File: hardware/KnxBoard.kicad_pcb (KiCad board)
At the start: 4 copper layers, 29.5 x 33.5 mm, 40 parts, among them J1 Conn_01x10, J2 Conn_01x12, J3 Conn_01x12, J4 Conn_01x02_Male, U1 NCN5130, U2 STM32L432KCUx, X1 FA-238

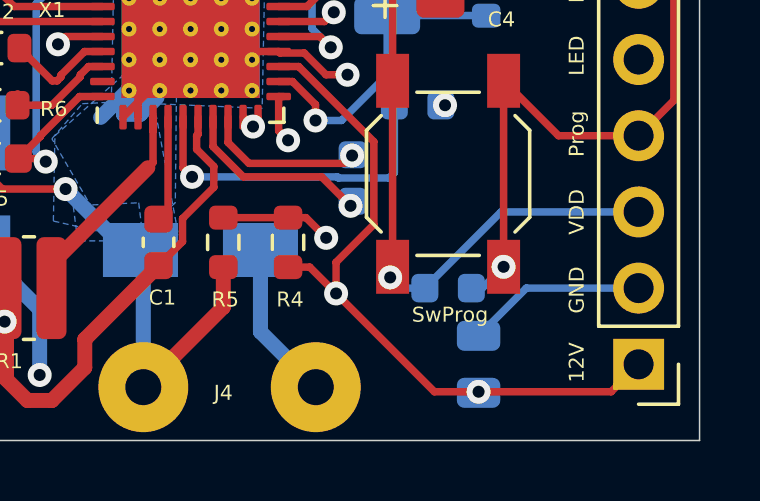
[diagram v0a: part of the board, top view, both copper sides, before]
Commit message: Project: Update to KiCad V6.0
Add also MCO to debug port (TODO: Need to route)
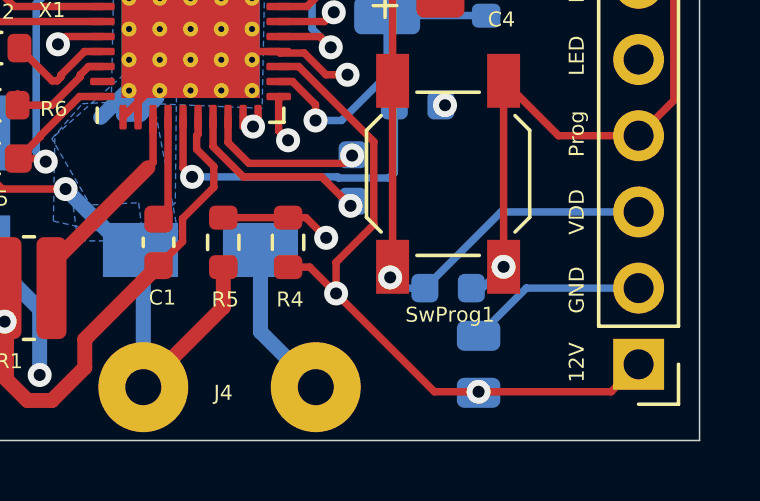
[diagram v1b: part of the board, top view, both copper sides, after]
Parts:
- R22: value 0 -> NOTMOUNT
- renumbered SwProg to SwProg1
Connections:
- J1 pad 8: Net-(J1-Pad8) -> MCO
- J2 pad 1: PC14 -> MCO
- U1 pad 22: Net-(U1-Pad22) -> unconnected-(U1-Pad22)
- U1 pad 39: Net-(U1-Pad39) -> unconnected-(U1-Pad39)
- U2 pad 2: PC14 -> MCO
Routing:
- net PC14: track 4.47 -> 0.00 mm
- net MCO: track 0.00 -> 4.47 mm
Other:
- net class Default removed

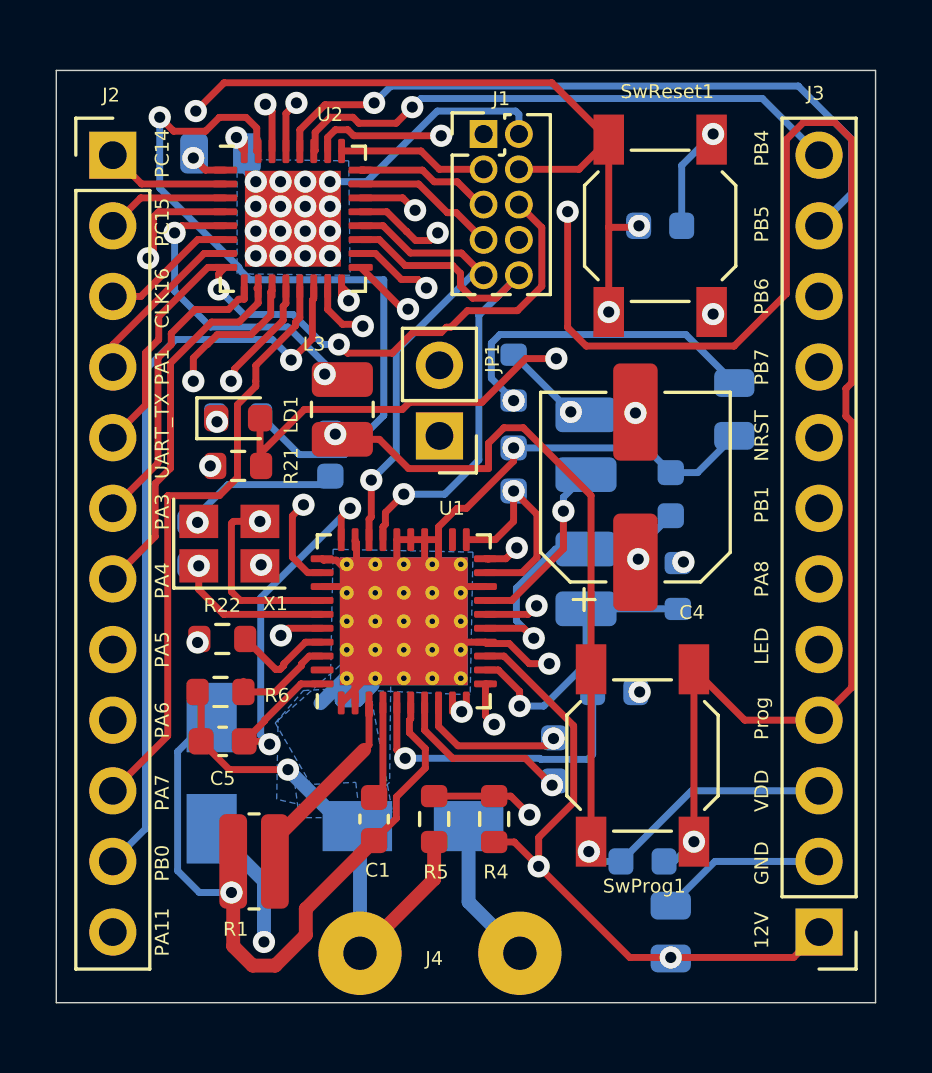
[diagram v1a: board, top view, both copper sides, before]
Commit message: Update pcb rules
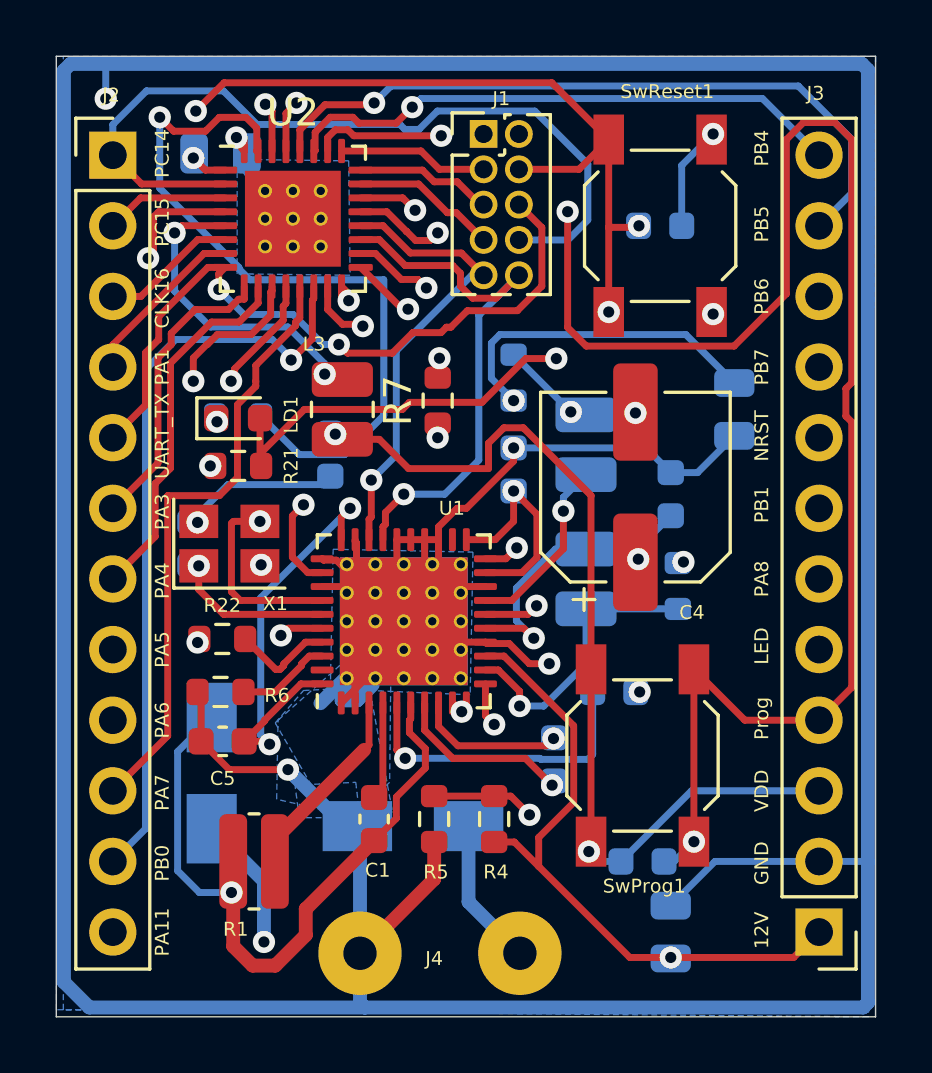
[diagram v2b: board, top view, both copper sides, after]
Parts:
- removed JP1: Jumper_2_Open, Connector_PinHeader_2.54mm:PinHeader_1x02_P2.54mm_Vertical
- added R7: 0, Resistor_SMD:R_0603_1608Metric, F.Cu at (148.8, 102.8)
- U2: footprint Package_DFN_QFN:QFN-32-1EP_5x5mm_P0.5mm_EP3.45x3.45mm -> Package_DFN_QFN:QFN-32-1EP_5x5mm_P0.5mm_EP3.45x3.45mm_ThermalVias
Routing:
- net GND: track 200.2 -> 329.6 mm, vias 28 -> 13
- net MCO: track 4.47 -> 29.6 mm
- net +3V3: track 49.2 -> 47.8 mm, vias 4 -> 5
- net VDD: vias 4 -> 5
- net +12V: vias 3 -> 2
- removed copper zone on In1.Cu, net GND
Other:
- board size 29.5 x 33.5 mm -> 29.5 x 34.5 mm

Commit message: Add CAD file for SMT32U575CIU6Q
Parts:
- added U2: STM32U575CIU6Q, KnxBoard:STM32U575CIU6Q, F.Cu at (143.0, 78.7)
- renumbered U2 to U3

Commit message: Work in progress
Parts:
- removed C21, C23, C5: 100nF 6.3V, Capacitor_SMD:C_0603_1608Metric
- removed C22: 10uF 6.3V ESR < 0.1ohm, Capacitor_SMD:C_0805_2012Metric
- removed C3: 100nF 50V, Capacitor_SMD:C_0603_1608Metric
- removed C41: 1uF 35V ESR < 2ohm, Capacitor_SMD:C_0603_1608Metric
- removed C8, C9: 10pF 6.3V, Capacitor_SMD:C_0603_1608Metric
- removed L3: 220uH, Inductor_SMD:L_1008_2520Metric
- removed R20: 10K 1/16w, Resistor_SMD:R_0603_1608Metric
- removed R22: NOTMOUNT, Resistor_SMD:R_0603_1608Metric
- removed R7: 0, Resistor_SMD:R_0603_1608Metric
- removed SwProg1, SwReset1: SW_Push, Button_Switch_SMD:SW_SPST_SKQG_WithStem
- removed U2: STM32U575CIU6Q, KnxBoard:STM32U575CIU6Q
- removed U3: STM32L432KCUx, Package_DFN_QFN:QFN-32-1EP_5x5mm_P0.5mm_EP3.45x3.45mm_ThermalVias
- added B1: Reset, Button_Switch_SMD:SW_SPST_SKQG_WithStem, F.Cu at (254.0, 104.1)
- added B2: KNX_PROG, Button_Switch_SMD:SW_SPST_SKQG_WithStem, F.Cu at (193.8, 87.4)
- added C12: 1uF 35V ESR < 2ohm, Capacitor_SMD:C_0603_1608Metric_Pad1.08x0.95mm_HandSolder, F.Cu at (219.4, 111.1)
- added C13: 220nF 50V, Capacitor_SMD:C_0603_1608Metric_Pad1.08x0.95mm_HandSolder, F.Cu at (227.6, 97.2)
- added C14: 47nF 50V, Capacitor_SMD:C_0603_1608Metric_Pad1.08x0.95mm_HandSolder, F.Cu at (240.0, 91.5)
- added C15: 100nF 6.3V, Capacitor_SMD:C_0603_1608Metric_Pad1.08x0.95mm_HandSolder, F.Cu at (232.4, 94.2)
- added C16: 10pF 6.3V, Capacitor_SMD:C_0603_1608Metric_Pad1.08x0.95mm_HandSolder, F.Cu at (223.4, 106.2)
- added C17: 10pF 6.3V, Capacitor_SMD:C_0603_1608Metric_Pad1.08x0.95mm_HandSolder, F.Cu at (242.8, 85.2)
- added C18: 100nF 6.3V, Capacitor_SMD:C_0603_1608Metric_Pad1.08x0.95mm_HandSolder, F.Cu at (181.9, 122.9)
- added C19: 10uF 6.3V ESR < 0.1ohm, Capacitor_SMD:C_0805_2012Metric_Pad1.18x1.45mm_HandSolder, F.Cu at (227.9, 94.5)
- added C3_25: 100nF, Capacitor_SMD:C_0603_1608Metric_Pad1.08x0.95mm_HandSolder, F.Cu at (272.5, 87.8)
- added C3_36: 100nF, Capacitor_SMD:C_0603_1608Metric_Pad1.08x0.95mm_HandSolder, F.Cu at (272.5, 85.2)
- added C3_48: 100nF, Capacitor_SMD:C_0603_1608Metric_Pad1.08x0.95mm_HandSolder, F.Cu at (268.2, 93.8)
- added C5_9: 100nF, Capacitor_SMD:C_0603_1608Metric_Pad1.08x0.95mm_HandSolder, F.Cu at (260.9, 102.0)
- added D0: D_Zener, Diode_SMD:D_SOD-323, F.Cu at (268.1, 96.5)
- added JP0: Bootloader, Jumper:SolderJumper-2_P1.3mm_Open_TrianglePad1.0x1.5mm, F.Cu at (255.8, 109.3)
- added JP1: Bootflash, Jumper:SolderJumper-2_P1.3mm_Open_TrianglePad1.0x1.5mm, F.Cu at (268.2, 85.8)
- added JP2: RESETB_NRST, Jumper:SolderJumper-2_P1.3mm_Open_TrianglePad1.0x1.5mm, F.Cu at (251.4, 111.8)
- added JP3: PWR_KNX_MCU, Jumper:SolderJumper-2_P1.3mm_Open_TrianglePad1.0x1.5mm, F.Cu at (200.7, 85.8)
- added TP1: KNX_RXD, TestPoint:TestPoint_Pad_D1.5mm, F.Cu at (185.8, 123.4)
- added TP2: KNX_TXD, TestPoint:TestPoint_Pad_D1.5mm, F.Cu at (190.8, 92.5)
- added U0: STM32U575CIU6Q, KnxBoard:STM32U575CIU6Q, F.Cu at (160.0, 91.4)
- C1: value 47nF 50V -> 100 nF; footprint Capacitor_SMD:C_0603_1608Metric -> Capacitor_SMD:C_0603_1608Metric_Pad1.08x0.95mm_HandSolder
- C10: value 10uF 6.3V ESR < 0.1ohm -> 100nF 50V; footprint Capacitor_SMD:C_0805_2012Metric -> Capacitor_SMD:C_0603_1608Metric_Pad1.08x0.95mm_HandSolder; moved to F.Cu
- C11: value 10uF 6.3V ESR < 0.1ohm -> 100uF 35V; footprint Capacitor_SMD:C_0805_2012Metric -> Capacitor_SMD:CP_Elec_6.3x7.7; moved to F.Cu
- C2: value 220nF 50V -> 10uF; footprint Capacitor_SMD:C_0603_1608Metric -> Capacitor_SMD:C_0603_1608Metric_Pad1.08x0.95mm_HandSolder; moved to F.Cu
- C20: value 100nF 6.3V -> 10uF 6.3V ESR < 0.1ohm; footprint Capacitor_SMD:C_0603_1608Metric -> Capacitor_SMD:C_0805_2012Metric_Pad1.18x1.45mm_HandSolder; moved to F.Cu
- C4: value 100uF 35V -> 1uF; footprint Capacitor_SMD:CP_Elec_6.3x7.7 -> Capacitor_SMD:C_0603_1608Metric_Pad1.08x0.95mm_HandSolder
- C6: value 100nF 6.3V -> 100nF; footprint Capacitor_SMD:C_0603_1608Metric -> Capacitor_SMD:C_0603_1608Metric_Pad1.08x0.95mm_HandSolder; moved to F.Cu
- D1, D2, L1, L2: moved to F.Cu
- J2, J3: value Conn_01x12 -> Conn_01x14; footprint Connector_PinHeader_2.54mm:PinHeader_1x12_P2.54mm_Vertical -> Connector_PinHeader_2.54mm:PinHeader_1x14_P2.54mm_Vertical
- R1: value 27R 1W -> NOTMOUNT; footprint Resistor_SMD:R_0612_1632Metric -> Resistor_SMD:R_0603_1608Metric
- R2: value 1R 1/16W -> 56K 1/16w; moved to F.Cu
- R3: value 1R 1/16W -> 499K 1/16w; moved to F.Cu
- R4: value 56K 1/16w -> 1R 1/16W
- R5: value 499K 1/16w -> 1R 1/16W
- R6: value NOTMOUNT -> 27R 1W; footprint Resistor_SMD:R_0603_1608Metric -> Resistor_SMD:R_0612_1632Metric
- moved C1 125.0 mm to (268.2, 88.8), turned to 0 degrees
- moved C2 117.7 mm to (268.2, 91.3), turned to 0 degrees
- moved R4 98.1 mm to (244.2, 87.8), turned to 0 degrees
- moved C4 95.5 mm to (251.4, 108.8), turned to 0 degrees
- moved R1 92.0 mm to (232.1, 99.8), turned to 0 degrees
- moved X1 90.6 mm to (230.3, 90.8)
- moved R5 90.5 mm to (236.6, 96.5), turned to 0 degrees
- moved R21 89.6 mm to (220.2, 62.0)
- moved D2 89.6 mm to (231.7, 86.3), turned to 0 degrees
- moved L1 86.0 mm to (238.2, 85.9), turned to 0 degrees
- moved R2 85.4 mm to (236.6, 94.0), turned to 0 degrees
- moved LD1 85.3 mm to (216.2, 62.1)
- moved L2 83.4 mm to (235.4, 90.4), turned to 0 degrees
- moved C10 81.8 mm to (240.0, 89.0), turned to 0 degrees
- moved D1 81.7 mm to (221.2, 102.7), turned to 0 degrees
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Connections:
- net /CLK0 renamed Net-(C16-Pad2)
- net /CLK1 renamed Net-(C17-Pad2)
- net /KNX+ renamed /KNXIFACE/KNX+
- C1 pad 1: Net-(C1-Pad1) -> NRST
- C1 pad 2: Net-(C1-Pad2) -> GNDREF
- C10 pad 1: +3V3 -> Net-(C10-Pad1)
- C10 pad 2: GND -> GNDREF
- C11 pad 1: +12V -> /KNXIFACE/Vfilt
- C11 pad 2: GND -> GNDREF
- C2 pad 1: Net-(C2-Pad1) -> VDD
- C2 pad 2: Net-(C2-Pad2) -> GNDREF
- C20 pad 1: NRST -> +3V3
- C20 pad 2: GND -> GNDREF
- C4 pad 1: /Vfilt -> VDD
- C4 pad 2: GND -> GNDREF
- D1 pad 1: Net-(C1-Pad2) -> Net-(C14-Pad2)
- D2 pad 2: GND -> GNDREF
- J1 pad 10: RXD -> GNDREF
- J1 pad 2: GND -> GNDREF
- J1 pad 3: UART_RX -> /MCU/DEBUG_JTDI
- J1 pad 4: NRST -> /MCU/DEBUG_JTMS-SWDIO
- J1 pad 5: SWCLK -> /MCU/DEBUG_JTCK-SWCLK
- J1 pad 6: UART_TX -> /MCU/DEBUG_JTDA-SWO
- J1 pad 7: SWDIO -> /MCU/DEBUG_UART_RX
- J1 pad 8: MCO -> /MCU/DEBUG_UART_TX
- J1 pad 9: TXD -> NRST
- J2 pad 1: MCO -> +12V
- J2 pad 10: PA7 -> /MCU/PA12
- J2 pad 11: PB0 -> /MCU/PA11
- J2 pad 12: PA11 -> /MCU/PB15
- J2 pad 2: PC15 -> GNDREF
- J2 pad 3: CLK16 -> VDD
- J2 pad 4: PA1 -> /MCU/PB8
- J2 pad 5: UART_TX -> /MCU/PB7
- J2 pad 6: PA3 -> /MCU/PB6
- J2 pad 7: PA4 -> /MCU/PA8
- J2 pad 8: PA5 -> /MCU/PB5
- J2 pad 9: PA6 -> /MCU/PB4
- J3 pad 1: +12V -> Led
- J3 pad 10: PB6 -> /MCU/PA5
- J3 pad 11: PB5 -> /MCU/PA6
- J3 pad 12: PB4 -> /MCU/PA7
- J3 pad 2: GND -> Prog
- J3 pad 3: VDD -> KNX_SAVEB
- J3 pad 4: Prog -> CLK16
- J3 pad 5: Led -> KNX_RESETB
- J3 pad 6: PA8 -> NRST
- J3 pad 7: PB1 -> /MCU/PA0
- J3 pad 8: NRST -> /MCU/PA1
- J3 pad 9: PB7 -> /MCU/PA4
- J4 pad 2: GND -> GNDREF
- LD1 pad 1: GND -> GNDREF
- LD1 pad 2: Led -> Net-(LD1-Pad2)
- R1 pad 2: Net-(C1-Pad2) -> GNDREF
- R2 pad 1: Net-(L1-Pad2) -> Net-(R2-Pad1)
- R2 pad 2: +3V3 -> +12V
- R21 pad 1: Net-(R21-Pad1) -> Led
- R21 pad 2: Led -> Net-(LD1-Pad2)
- R3 pad 1: Net-(L2-Pad2) -> GNDREF
- R3 pad 2: +12V -> Net-(R2-Pad1)
- R4 pad 1: Net-(R4-Pad1) -> Net-(L1-Pad2)
- R5 pad 1: GND -> Net-(L2-Pad2)
- R5 pad 2: Net-(R4-Pad1) -> +3V3
- R6 pad 2: GND -> Net-(C14-Pad2)
- U1 pad 1: GND -> GNDREF
- U1 pad 10: /Vfilt -> /KNXIFACE/Vfilt
- U1 pad 11: Net-(R4-Pad1) -> Net-(R2-Pad1)
- U1 pad 12: Net-(L2-Pad2) -> Net-(L1-Pad2)
- U1 pad 14: GND -> GNDREF
- U1 pad 15: Net-(L2-Pad1) -> Net-(L1-Pad1)
- U1 pad 16: /Vfilt -> /KNXIFACE/Vfilt
- U1 pad 17: Net-(L1-Pad1) -> Net-(L2-Pad1)
- U1 pad 18: GND -> GNDREF
- U1 pad 2: GND -> GNDREF
- U1 pad 20: Net-(L1-Pad2) -> Net-(L2-Pad2)
- U1 pad 23: GND -> Net-(U1-Pad23)
- U1 pad 24: GND -> Net-(U1-Pad23)
- U1 pad 25: GND -> Net-(U1-Pad23)
- U1 pad 26: GND -> Net-(U1-Pad23)
- U1 pad 27: RXD -> /KNXIFACE/KNX_RXD
- U1 pad 28: TXD -> /KNXIFACE/KNX_TXD
- U1 pad 29: GND -> Net-(U1-Pad23)
- U1 pad 3: Net-(R1-Pad1) -> Net-(R6-Pad1)
- U1 pad 36: PA11 -> KNX_SAVEB
- U1 pad 37: Net-(R22-Pad2) -> KNX_RESETB
- U1 pad 38: Net-(R6-Pad1) -> Net-(R1-Pad1)
- U1 pad 4: Net-(C1-Pad1) -> Net-(C14-Pad1)
- U1 pad 5: Net-(C3-Pad1) -> Net-(C10-Pad1)
- U1 pad 6: Net-(C1-Pad2) -> Net-(C14-Pad2)
- U1 pad 7: Net-(C2-Pad1) -> Net-(C13-Pad1)
- U1 pad 8: Net-(C2-Pad2) -> Net-(C13-Pad2)
- U1 pad 9: /Vfilt -> /KNXIFACE/Vfilt
- X1 pad 2: GND -> GNDREF
- X1 pad 4: GND -> GNDREF
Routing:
- net GND: track 329.6 -> 0.00 mm, vias 13 -> 0
- net Prog: track 69.4 -> 0.00 mm, vias 3 -> 0
- net VDD: track 66.9 -> 0.00 mm, vias 5 -> 0
- net NRST: track 65.9 -> 0.00 mm, vias 5 -> 0
- net Net-(R21-Pad1): track 52.8 -> 0.00 mm, vias 2 -> 0
- net +3V3: track 47.8 -> 0.00 mm, vias 5 -> 0
- net /MCU/PA6: track 0.00 -> 40.7 mm
- net +12V: track 40.3 -> 0.00 mm, vias 2 -> 0
- net PA11: track 38.0 -> 0.00 mm, vias 2 -> 0
- net Led: track 31.9 -> 0.00 mm, vias 1 -> 0
- net PB7: track 30.4 -> 0.00 mm, vias 1 -> 0
- net MCO: track 29.6 -> 0.00 mm
- net Net-(R20-Pad1): track 27.4 -> 0.00 mm, vias 1 -> 0
- net PB0: track 27.2 -> 0.00 mm, vias 1 -> 0
- net PB6: track 26.0 -> 0.00 mm, vias 1 -> 0
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- removed copper zone on B.Cu, net GND
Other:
- board outline removed
- board text removed: "12V"
- board text removed: "By Fabien Proriol"
- board text removed: "CLK16"
- board text removed: "GND"
- board text removed: "KnxBoard V2.0"
- board text removed: "LED"
- board text removed: "NRST"
- board text removed: "PA1"
- board text removed: "PA11"
- board text removed: "PA3"
- board text removed: "PA4"
- board text removed: "PA5"
- board text removed: "PA6"
- board text removed: "PA7"
- board text removed: "PA8"
- board text removed: "PB0"
- board text removed: "PB1"
- board text removed: "PB4"
- board text removed: "PB5"
- board text removed: "PB6"
- board text removed: "PB7"
- board text removed: "PC14"
- board text removed: "PC15"
- board text removed: "Prog"
- board text removed: "UART_TX"
- board text removed: "VDD"

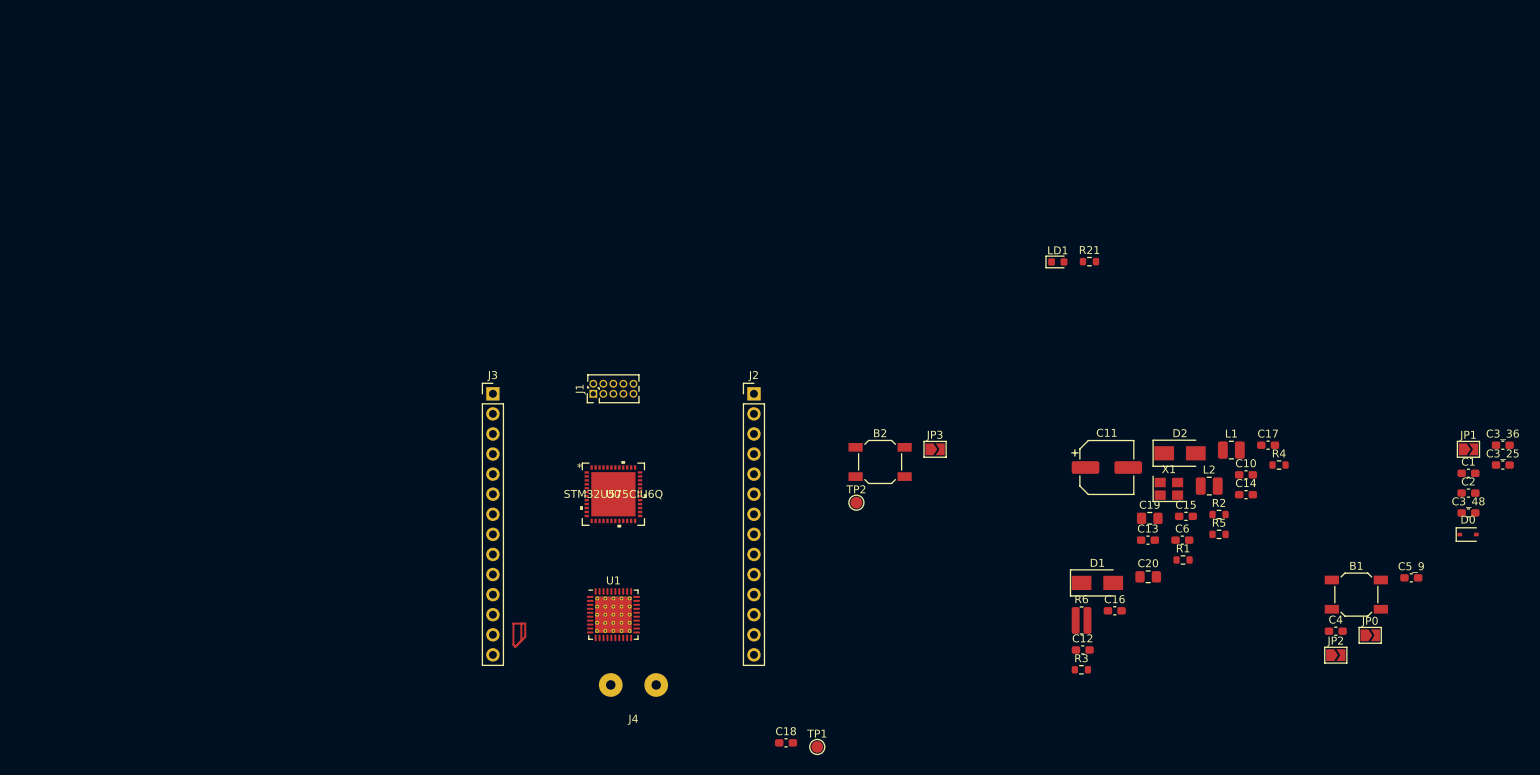
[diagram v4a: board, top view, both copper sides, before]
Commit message: Switch to STM32U575CIT6
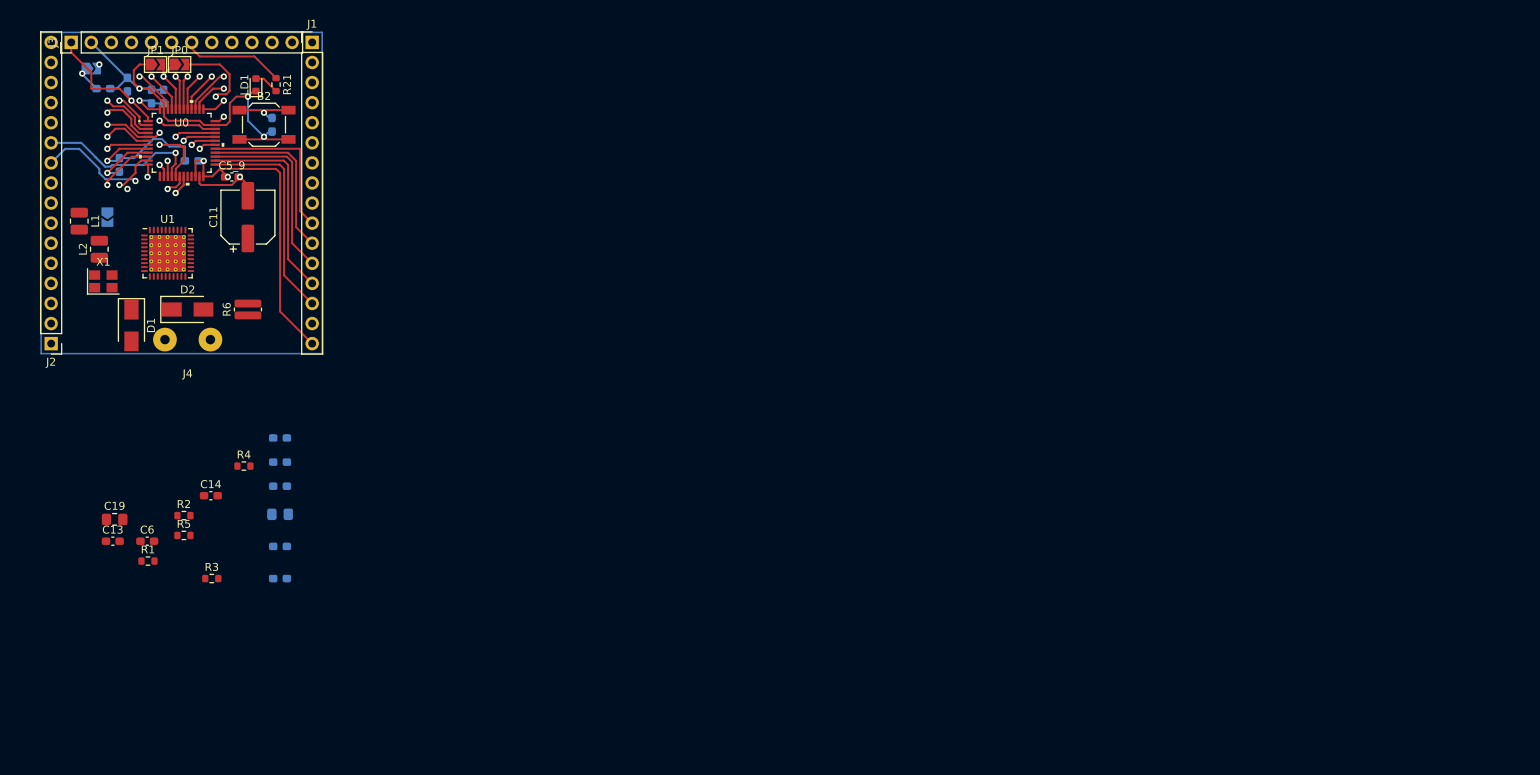
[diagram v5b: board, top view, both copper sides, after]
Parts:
- removed B1: Reset, Button_Switch_SMD:SW_SPST_SKQG_WithStem
- removed D0: D_Zener, Diode_SMD:D_SOD-323
- removed TP1: KNX_RXD, TestPoint:TestPoint_Pad_D1.5mm
- removed TP2: KNX_TXD, TestPoint:TestPoint_Pad_D1.5mm
- C1, C10, C12, C15, C16, C17, C18, C2, C20, C3_25, C3_36, C3_48, C4, JP2, JP3: moved to B.Cu
- J1: value Conn_01x10 -> Conn_01x16; footprint Connector_PinHeader_1.27mm:PinHeader_2x05_P1.27mm_Vertical -> Connector_PinHeader_2.54mm:PinHeader_1x16_P2.54mm_Vertical
- J2: value Conn_01x14 -> Conn_01x16; footprint Connector_PinHeader_2.54mm:PinHeader_1x14_P2.54mm_Vertical -> Connector_PinHeader_2.54mm:PinHeader_1x16_P2.54mm_Vertical
- J3: value Conn_01x14 -> Conn_01x12; footprint Connector_PinHeader_2.54mm:PinHeader_1x14_P2.54mm_Vertical -> Connector_PinHeader_2.54mm:PinHeader_1x12_P2.54mm_Vertical
- U0: value STM32U575CIU6Q -> STM32U575CIT6; footprint KnxBoard:STM32U575CIU6Q -> KnxBoard:STM32U575CIT6
- moved C3_36 179.9 mm to (98.6, 39.6), turned to 90 degrees
- moved C1 179.4 mm to (95.5, 40.1)
- moved C3_25 179.1 mm to (97.5, 49.8), turned to 90 degrees
- moved C3_48 174.7 mm to (101.6, 41.1), turned to 90 degrees
- moved JP2 174.0 mm to (94.0, 37.6)
- moved JP1 173.1 mm to (102.1, 37.1)
- moved JP0 167.0 mm to (105.2, 37.1)
- moved C2 166.9 mm to (106.7, 49.3), turned to 180 degrees
- moved C4 163.0 mm to (103.1, 41.1), turned to 90 degrees
- moved C5_9 157.6 mm to (111.8, 51.3)
- moved L1 148.6 mm to (92.5, 56.9), turned to -90 degrees
- moved L2 143.6 mm to (95.0, 60.5), turned to 90 degrees
- moved X1 137.3 mm to (95.5, 64.5)
- moved C19 130.9 mm to (96.9, 94.6)
- moved C6 130.9 mm to (101.1, 97.4)
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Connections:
- B2 pad 2: Prog -> GNDREF
- J1 pad 1: VDD -> /MCU/PB4
- J1 pad 10: GNDREF -> /MCU/PA8
- J1 pad 2: GNDREF -> /MCU/DEBUG_JTDA-SWO
- J1 pad 4: /MCU/DEBUG_JTMS-SWDIO -> /MCU/DEBUG_JTCK-SWCLK
- J1 pad 5: /MCU/DEBUG_JTCK-SWCLK -> /MCU/DEBUG_JTMS-SWDIO
- J1 pad 6: /MCU/DEBUG_JTDA-SWO -> /MCU/PA12
- J1 pad 7: /MCU/DEBUG_UART_RX -> /MCU/PA11
- J1 pad 8: /MCU/DEBUG_UART_TX -> /MCU/DEBUG_UART_RX
- J1 pad 9: NRST -> /MCU/DEBUG_UART_TX
- J2 pad 10: /MCU/PA12 -> /MCU/PA7
- J2 pad 11: /MCU/PA11 -> /MCU/PA6
- J2 pad 12: /MCU/PB15 -> /MCU/PA5
- J2 pad 13: /MCU/PB14 -> /MCU/PA4
- J2 pad 14: /MCU/PB13 -> /MCU/PA1
- J2 pad 4: /MCU/PB8 -> KNX_RXD
- J2 pad 5: /MCU/PB7 -> KNX_TXD
- J2 pad 6: /MCU/PB6 -> KNX_RESETB
- J2 pad 7: /MCU/PA8 -> KNX_SAVEB
- J2 pad 8: /MCU/PB5 -> /MCU/PB1
- J2 pad 9: /MCU/PB4 -> /MCU/PB0
- J3 pad 1: Led -> VDD
- J3 pad 10: /MCU/PA5 -> /MCU/PB7
- J3 pad 11: /MCU/PA6 -> /MCU/PB6
- J3 pad 12: /MCU/PA7 -> /MCU/PB5
- J3 pad 2: Prog -> GNDREF
- J3 pad 3: KNX_SAVEB -> /MCU/PH1
- J3 pad 5: KNX_RESETB -> /MCU/PC15
- J3 pad 6: NRST -> Prog
- J3 pad 7: /MCU/PA0 -> Led
- J3 pad 8: /MCU/PA1 -> /MCU/PB9
- J3 pad 9: /MCU/PA4 -> /MCU/PB8
- JP2 pad 2: KNX_RESETB -> /MCU/PH1
- U0 pad 12: /KNXIFACE/KNX_RXD -> KNX_RXD
- U0 pad 13: /KNXIFACE/KNX_TXD -> KNX_TXD
- U0 pad 20: unconnected-(U0-Pad20) -> KNX_SAVEB
- U0 pad 21: unconnected-(U0-Pad21) -> KNX_RESETB
- U0 pad 22: GNDREF -> VDD
- U0 pad 23: unconnected-(U0-Pad23) -> GNDREF
- U0 pad 24: GNDREF -> VDD
- U0 pad 25: VDD -> /MCU/PB12
- U0 pad 4: KNX_SAVEB -> /MCU/PC15
- U0 pad 46: unconnected-(U0-Pad46) -> /MCU/PB9
- U0 pad 6: KNX_RESETB -> /MCU/PH1
- U1 pad 23: Net-(U1-Pad23) -> GND
- U1 pad 24: Net-(U1-Pad23) -> GND
- U1 pad 25: Net-(U1-Pad23) -> GND
- U1 pad 26: Net-(U1-Pad23) -> GND
- U1 pad 27: /KNXIFACE/KNX_RXD -> KNX_RXD
- U1 pad 28: /KNXIFACE/KNX_TXD -> KNX_TXD
- U1 pad 29: Net-(U1-Pad23) -> GND
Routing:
- net VDD: track 0.00 -> 115.2 mm, vias 0 -> 7
- net GNDREF: track 0.00 -> 100.1 mm, vias 0 -> 5
- net Prog: track 0.00 -> 48.2 mm, vias 0 -> 2
- net Led: track 0.00 -> 32.8 mm, vias 0 -> 1
- net CLK16: track 0.00 -> 28.8 mm, vias 0 -> 3
- net /MCU/PB12: track 0.00 -> 27.4 mm
- net /MCU/DEBUG_JTMS-SWDIO: track 0.00 -> 27.3 mm, vias 0 -> 1
- net /MCU/PA7: track 0.00 -> 27.2 mm, vias 0 -> 2
- net /MCU/PA4: track 0.00 -> 26.6 mm, vias 0 -> 1
- net /MCU/PA0: track 0.00 -> 26.4 mm, vias 0 -> 1
- net /MCU/PA1: track 0.00 -> 26.2 mm, vias 0 -> 1
- net /MCU/PB13: track 0.00 -> 25.7 mm
- net NRST: track 0.00 -> 24.4 mm, vias 0 -> 2
- net /MCU/PH1: track 0.00 -> 24.1 mm, vias 0 -> 2
- net /MCU/PA12: track 0.00 -> 23.9 mm, vias 0 -> 1
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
